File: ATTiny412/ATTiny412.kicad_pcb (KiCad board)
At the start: 2 copper layers, 18 x 24.3 mm, 27 parts, among them J1 Conn_01x04, J2 Conn_01x02, J3 Conn_01x04, U1 AP2204K-ADJ

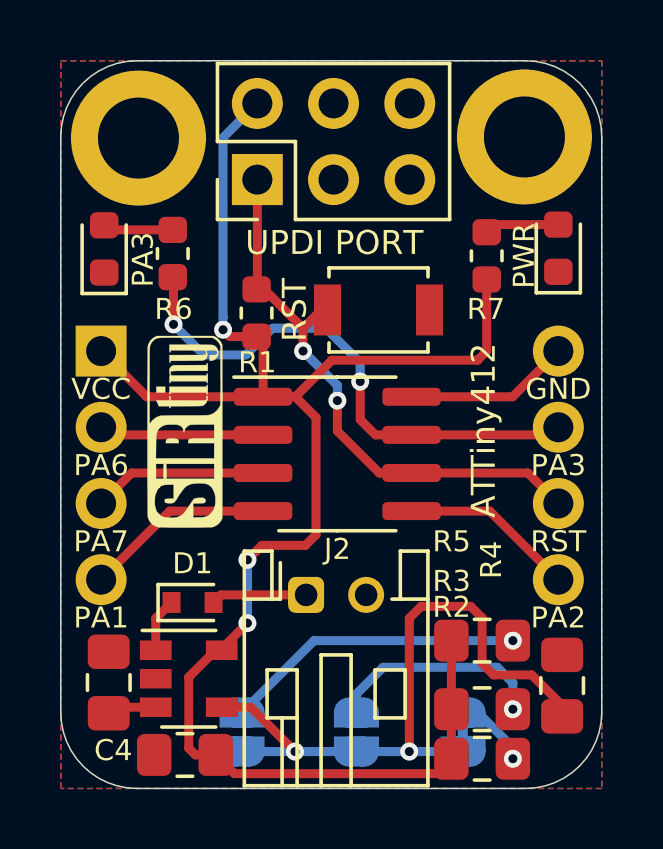
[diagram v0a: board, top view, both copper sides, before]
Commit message: Spacings Updated
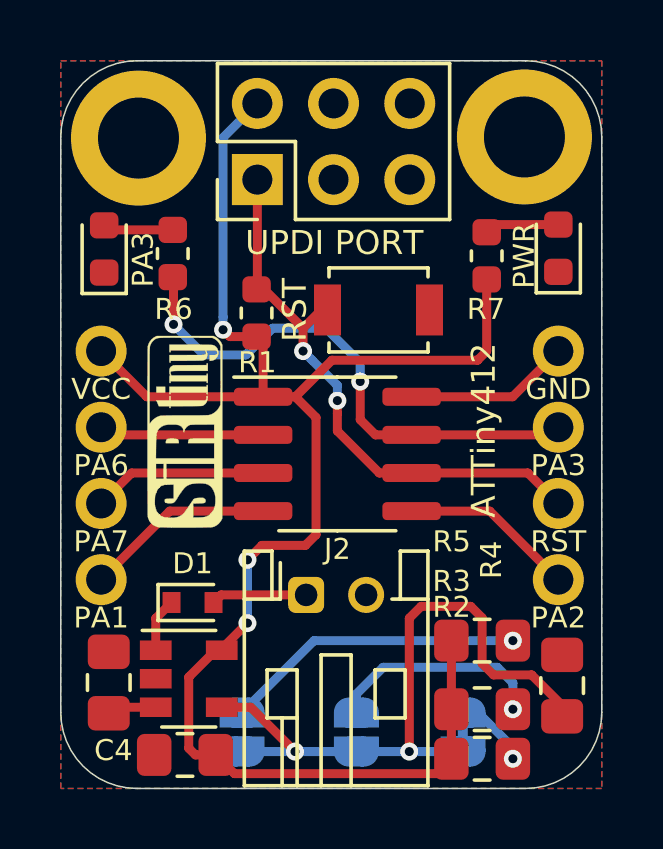
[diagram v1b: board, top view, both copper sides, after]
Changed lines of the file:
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@@
     (31 B.Cu signal)
     (32 B.Adhes user)
-    (33 F.Adhes user hide)
-    (34 B.Paste user hide)
-    (35 F.Paste user hide)
+    (33 F.Adhes user)
+    (34 B.Paste user)
+    (35 F.Paste user)
     (36 B.SilkS user)
     (37 F.SilkS user)
-    (38 B.Mask user hide)
-    (39 F.Mask user hide)
+    (38 B.Mask user)
+    (39 F.Mask user)
     (40 Dwgs.User user)
     (41 Cmts.User user hide)
@@
     (mod_text_size 1 1)
     (mod_text_width 0.15)
-    (pad_size 1.2 1.2)
-    (pad_drill 0.75)
+    (pad_size 1.7 1.7)
+    (pad_drill 1)
     (pad_to_mask_clearance 0.051)
     (solder_mask_min_width 0.25)
@@
     (add_net VIN)
   )
+  (module Connector_PinHeader_2.54mm:PinHeader_1x04_P2.54mm_Vertical (layer B.Cu)
+    (at 162.052 117.348 180)
+    (descr "Through hole straight pin header, 1x04, 2.54mm pitch, single row")
+    (tags "Through hole pin header THT 1x04 2.54mm single row")
+    (fp_text reference J1 (at 0 2.33 180) (layer B.SilkS) hide
+      (effects (font (size 1 1) (thickness 0.15)) (justify mirror))
+    )
+    (fp_text value Conn_01x04 (at 0 -9.95 180) (layer B.Fab)
+      (effects (font (size 1 1) (thickness 0.15)) (justify mirror))
+    )
+    (fp_text user %R (at 0 -3.81 90) (layer B.Fab)
+      (effects (font (size 1 1) (thickness 0.15)) (justify mirror))
+    )
+    (fp_line (start 1.8 1.8) (end -1.8 1.8) (layer B.CrtYd) (width 0.05))
+    (fp_line (start 1.8 -9.4) (end 1.8 1.8) (layer B.CrtYd) (width 0.05))
+    (fp_line (start -1.8 -9.4) (end 1.8 -9.4) (layer B.CrtYd) (width 0.05))
+    (fp_line (start -1.8 1.8) (end -1.8 -9.4) (layer B.CrtYd) (width 0.05))
+    (fp_line (start -1.27 0.635) (end -0.635 1.27) (layer B.Fab) (width 0.1))
+    (fp_line (start -1.27 -8.89) (end -1.27 0.635) (layer B.Fab) (width 0.1))
+    (fp_line (start 1.27 -8.89) (end -1.27 -8.89) (layer B.Fab) (width 0.1))
+    (fp_line (start 1.27 1.27) (end 1.27 -8.89) (layer B.Fab) (width 0.1))
+    (fp_line (start -0.635 1.27) (end 1.27 1.27) (layer B.Fab) (width 0.1))
+    (pad 4 thru_hole oval (at 0 -7.62 180) (size 1.7 1.7) (drill 1) (layers *.Cu *.Mask)
+      (net 11 PA1))
+    (pad 3 thru_hole oval (at 0 -5.08 180) (size 1.7 1.7) (drill 1) (layers *.Cu *.Mask)
+      (net 12 PA7))
+    (pad 2 thru_hole oval (at 0 -2.54 180) (size 1.7 1.7) (drill 1) (layers *.Cu *.Mask)
+      (net 13 PA6))
+    (pad 1 thru_hole circle (at 0 0 180) (size 1.7 1.7) (drill 1) (layers *.Cu *.Mask)
+      (net 2 VCC))
+    (model ${KISYS3DMOD}/Connector_PinHeader_2.54mm.3dshapes/PinHeader_1x04_P2.54mm_Vertical.wrl
+      (at (xyz 0 0 0))
+      (scale (xyz 1 1 1))
+      (rotate (xyz 0 0 0))
+    )
+  )
+  (module Connector_PinHeader_2.54mm:PinHeader_1x04_P2.54mm_Vertical (layer B.Cu)
+    (at 177.292 117.348 180)
+    (descr "Through hole straight pin header, 1x04, 2.54mm pitch, single row")
+    (tags "Through hole pin header THT 1x04 2.54mm single row")
+    (fp_text reference J3 (at 0 2.33 180) (layer B.SilkS) hide
+      (effects (font (size 1 1) (thickness 0.15)) (justify mirror))
+    )
+    (fp_text value Conn_01x04 (at 0 -9.95 180) (layer B.Fab)
+      (effects (font (size 1 1) (thickness 0.15)) (justify mirror))
+    )
+    (fp_text user %R (at 0 -3.81 90) (layer B.Fab)
+      (effects (font (size 1 1) (thickness 0.15)) (justify mirror))
+    )
+    (fp_line (start 1.8 1.8) (end -1.8 1.8) (layer B.CrtYd) (width 0.05))
+    (fp_line (start 1.8 -9.4) (end 1.8 1.8) (layer B.CrtYd) (width 0.05))
+    (fp_line (start -1.8 -9.4) (end 1.8 -9.4) (layer B.CrtYd) (width 0.05))
+    (fp_line (start -1.8 1.8) (end -1.8 -9.4) (layer B.CrtYd) (width 0.05))
+    (fp_line (start -1.27 0.635) (end -0.635 1.27) (layer B.Fab) (width 0.1))
+    (fp_line (start -1.27 -8.89) (end -1.27 0.635) (layer B.Fab) (width 0.1))
+    (fp_line (start 1.27 -8.89) (end -1.27 -8.89) (layer B.Fab) (width 0.1))
+    (fp_line (start 1.27 1.27) (end 1.27 -8.89) (layer B.Fab) (width 0.1))
+    (fp_line (start -0.635 1.27) (end 1.27 1.27) (layer B.Fab) (width 0.1))
+    (pad 4 thru_hole oval (at 0 -7.62 180) (size 1.7 1.7) (drill 1) (layers *.Cu *.Mask)
+      (net 14 PA2))
+    (pad 3 thru_hole oval (at 0 -5.08 180) (size 1.7 1.7) (drill 1) (layers *.Cu *.Mask)
+      (net 5 RST))
+    (pad 2 thru_hole oval (at 0 -2.54 180) (size 1.7 1.7) (drill 1) (layers *.Cu *.Mask)
+      (net 15 PA3))
+    (pad 1 thru_hole circle (at 0 0 180) (size 1.7 1.7) (drill 1) (layers *.Cu *.Mask)
+      (net 4 GND))
+    (model ${KISYS3DMOD}/Connector_PinHeader_2.54mm.3dshapes/PinHeader_1x04_P2.54mm_Vertical.wrl
+      (at (xyz 0 0 0))
+      (scale (xyz 1 1 1))
+      (rotate (xyz 0 0 0))
+    )
+  )
   (module Jumper:SolderJumper-2_P1.3mm_Bridged_RoundedPad1.0x1.5mm (layer B.Cu)
     (at 174.117 130.048 270)
@@
       (at (xyz 0 0 0))
       (scale (xyz 1 1 1))
-      (rotate (xyz 0 0 0))
-    )
-  )
-  (module Connector_PinHeader_2.54mm:PinHeader_1x04_P2.54mm_Vertical (layer B.Cu)
-    (at 177.292 117.348 180)
-    (descr "Through hole straight pin header, 1x04, 2.54mm pitch, single row")
-    (tags "Through hole pin header THT 1x04 2.54mm single row")
-    (fp_text reference J3 (at 0 2.33) (layer B.SilkS) hide
-      (effects (font (size 1 1) (thickness 0.15)) (justify mirror))
-    )
-    (fp_text value Conn_01x04 (at 0 -9.95) (layer B.Fab)
-      (effects (font (size 1 1) (thickness 0.15)) (justify mirror))
-    )
-    (fp_text user %R (at 0 -3.81 270) (layer B.Fab)
-      (effects (font (size 1 1) (thickness 0.15)) (justify mirror))
-    )
-    (fp_line (start 1.8 1.8) (end -1.8 1.8) (layer B.CrtYd) (width 0.05))
-    (fp_line (start 1.8 -9.4) (end 1.8 1.8) (layer B.CrtYd) (width 0.05))
-    (fp_line (start -1.8 -9.4) (end 1.8 -9.4) (layer B.CrtYd) (width 0.05))
-    (fp_line (start -1.8 1.8) (end -1.8 -9.4) (layer B.CrtYd) (width 0.05))
-    (fp_line (start -1.33 1.33) (end 0 1.33) (layer B.SilkS) (width 0.12))
-    (fp_line (start -1.33 0) (end -1.33 1.33) (layer B.SilkS) (width 0.12))
-    (fp_line (start -1.33 -1.27) (end 1.33 -1.27) (layer B.SilkS) (width 0.12))
-    (fp_line (start 1.33 -1.27) (end 1.33 -8.95) (layer B.SilkS) (width 0.12))
-    (fp_line (start -1.33 -1.27) (end -1.33 -8.95) (layer B.SilkS) (width 0.12))
-    (fp_line (start -1.33 -8.95) (end 1.33 -8.95) (layer B.SilkS) (width 0.12))
-    (fp_line (start -1.27 0.635) (end -0.635 1.27) (layer B.Fab) (width 0.1))
-    (fp_line (start -1.27 -8.89) (end -1.27 0.635) (layer B.Fab) (width 0.1))
-    (fp_line (start 1.27 -8.89) (end -1.27 -8.89) (layer B.Fab) (width 0.1))
-    (fp_line (start 1.27 1.27) (end 1.27 -8.89) (layer B.Fab) (width 0.1))
-    (fp_line (start -0.635 1.27) (end 1.27 1.27) (layer B.Fab) (width 0.1))
-    (pad 4 thru_hole oval (at 0 -7.62 180) (size 1.7 1.7) (drill 1) (layers *.Cu *.Mask)
-      (net 14 PA2))
-    (pad 3 thru_hole oval (at 0 -5.08 180) (size 1.7 1.7) (drill 1) (layers *.Cu *.Mask)
-      (net 5 RST))
-    (pad 2 thru_hole oval (at 0 -2.54 180) (size 1.7 1.7) (drill 1) (layers *.Cu *.Mask)
-      (net 15 PA3))
-    (pad 1 thru_hole circle (at 0 0 180) (size 1.7 1.7) (drill 1) (layers *.Cu *.Mask)
-      (net 4 GND))
-    (model ${KISYS3DMOD}/Connector_PinHeader_2.54mm.3dshapes/PinHeader_1x04_P2.54mm_Vertical.wrl
-      (at (xyz 0 0 0))
-      (scale (xyz 1 1 1))
-      (rotate (xyz 0 0 0))
-    )
-  )
-  (module Connector_PinHeader_2.54mm:PinHeader_1x04_P2.54mm_Vertical (layer B.Cu)
-    (at 162.052 117.348 180)
-    (descr "Through hole straight pin header, 1x04, 2.54mm pitch, single row")
-    (tags "Through hole pin header THT 1x04 2.54mm single row")
-    (fp_text reference J1 (at 0 2.33) (layer B.SilkS) hide
-      (effects (font (size 1 1) (thickness 0.15)) (justify mirror))
-    )
-    (fp_text value Conn_01x04 (at 0 -9.95) (layer B.Fab)
-      (effects (font (size 1 1) (thickness 0.15)) (justify mirror))
-    )
-    (fp_text user %R (at 0 -3.81 270) (layer B.Fab)
-      (effects (font (size 1 1) (thickness 0.15)) (justify mirror))
-    )
-    (fp_line (start 1.8 1.8) (end -1.8 1.8) (layer B.CrtYd) (width 0.05))
-    (fp_line (start 1.8 -9.4) (end 1.8 1.8) (layer B.CrtYd) (width 0.05))
-    (fp_line (start -1.8 -9.4) (end 1.8 -9.4) (layer B.CrtYd) (width 0.05))
-    (fp_line (start -1.8 1.8) (end -1.8 -9.4) (layer B.CrtYd) (width 0.05))
-    (fp_line (start -1.33 1.33) (end 0 1.33) (layer B.SilkS) (width 0.12))
-    (fp_line (start -1.33 0) (end -1.33 1.33) (layer B.SilkS) (width 0.12))
-    (fp_line (start -1.33 -1.27) (end 1.33 -1.27) (layer B.SilkS) (width 0.12))
-    (fp_line (start 1.33 -1.27) (end 1.33 -8.95) (layer B.SilkS) (width 0.12))
-    (fp_line (start -1.33 -1.27) (end -1.33 -8.95) (layer B.SilkS) (width 0.12))
-    (fp_line (start -1.33 -8.95) (end 1.33 -8.95) (layer B.SilkS) (width 0.12))
-    (fp_line (start -1.27 0.635) (end -0.635 1.27) (layer B.Fab) (width 0.1))
-    (fp_line (start -1.27 -8.89) (end -1.27 0.635) (layer B.Fab) (width 0.1))
-    (fp_line (start 1.27 -8.89) (end -1.27 -8.89) (layer B.Fab) (width 0.1))
-    (fp_line (start 1.27 1.27) (end 1.27 -8.89) (layer B.Fab) (width 0.1))
-    (fp_line (start -0.635 1.27) (end 1.27 1.27) (layer B.Fab) (width 0.1))
-    (pad 4 thru_hole oval (at 0 -7.62 180) (size 1.7 1.7) (drill 1) (layers *.Cu *.Mask)
-      (net 11 PA1))
-    (pad 3 thru_hole oval (at 0 -5.08 180) (size 1.7 1.7) (drill 1) (layers *.Cu *.Mask)
-      (net 12 PA7))
-    (pad 2 thru_hole oval (at 0 -2.54 180) (size 1.7 1.7) (drill 1) (layers *.Cu *.Mask)
-      (net 13 PA6))
-    (pad 1 thru_hole rect (at 0 0 180) (size 1.7 1.7) (drill 1) (layers *.Cu *.Mask)
-      (net 2 VCC))
-    (model ${KISYS3DMOD}/Connector_PinHeader_2.54mm.3dshapes/PinHeader_1x04_P2.54mm_Vertical.wrl
-      (at (xyz 0 0 0))
-      (scale (xyz 1 1 1))
